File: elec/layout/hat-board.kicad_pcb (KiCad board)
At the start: 2 copper layers, 108 x 115.9 mm, 82 parts, among them P1 HatButtonAntenna, U1 _NXP_Semicon_PN5321A3HN_C106_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, U10 _OPSCO_Optoelectronics_SK6805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, U11 _OPSCO_Optoelectronics_SK6805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, U12 _OPSCO_Optoelectronics_SK6805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, U13 _OPSCO_Optoelectronics_SK6805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, U14 _OPSCO_Optoelectronics_SK6805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, U15 _OPSCO_Optoelectronics_SK6805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, U16 _OPSCO_Optoelectronics_SK6805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, U17 _OPSCO_Optoelectronics_SK6805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, U18 _OPSCO_Optoelectronics_SK6805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, U19 _OPSCO_Optoelectronics_SK6805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, U2 _OPSCO_Optoelectronics_SK6805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, U20 _OPSCO_Optoelectronics_SK6805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, U21 _OPSCO_Optoelectronics_SK6805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, U22 _OPSCO_Optoelectronics_SK6805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, U23 _OPSCO_Optoelectronics_SK6805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, U24 _OPSCO_Optoelectronics_SK6805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, U25 _Microchip_Tech_CAP1188_1_CP_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, U3 _OPSCO_Optoelectronics_SK6805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, U4 _OPSCO_Optoelectronics_SK6805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, U5 _OPSCO_Optoelectronics_SK6805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, U6 _OPSCO_Optoelectronics_SK6805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, U7 _OPSCO_Optoelectronics_SK6805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, U8 _OPSCO_Optoelectronics_SK6805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, U9 _OPSCO_Optoelectronics_SK6805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

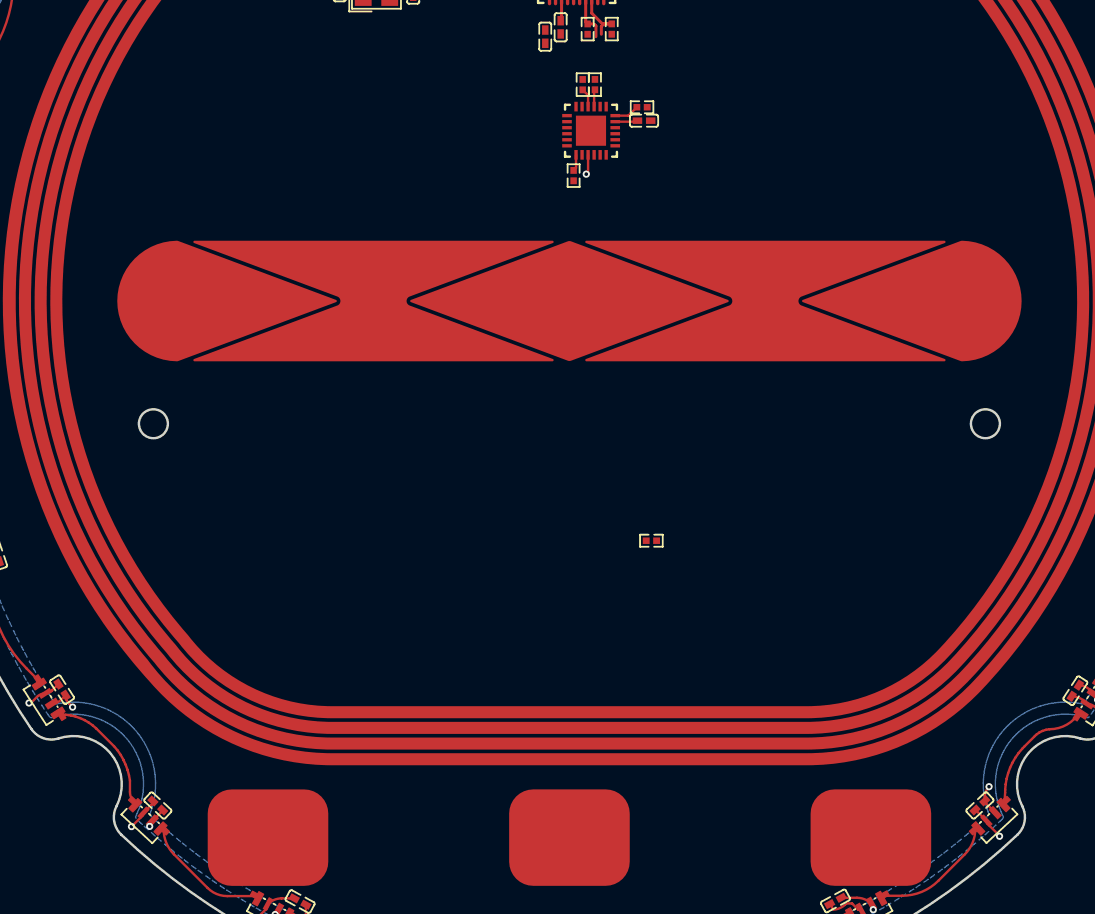
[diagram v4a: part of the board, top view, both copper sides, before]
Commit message: fixed hat-footprint
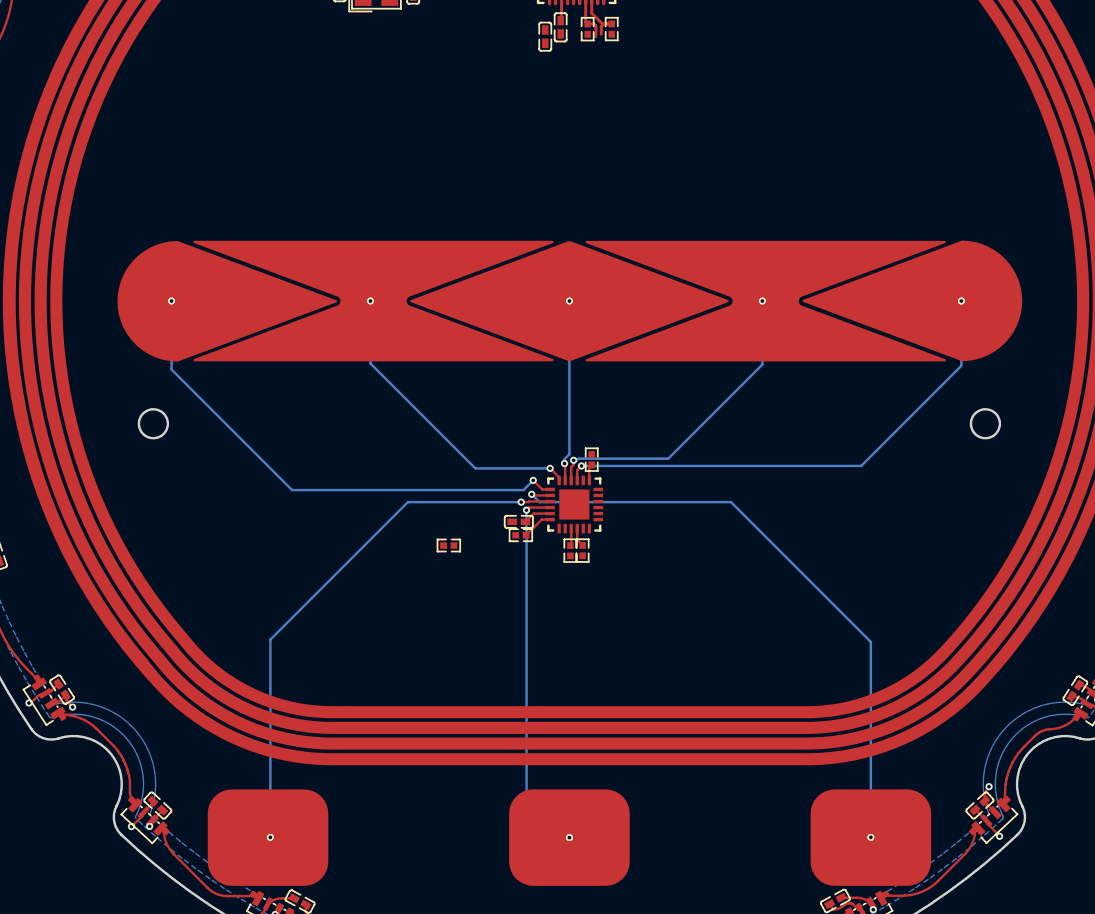
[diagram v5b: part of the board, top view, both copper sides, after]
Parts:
- moved R8 38.7 mm to (151.9, 111.8), turned to -90 degrees
- moved R7 38.6 mm to (152.9, 111.8), turned to -90 degrees
- moved R10 36.9 mm to (147.8, 110.5), turned to 180 degrees
- moved C42 34.9 mm to (147.6, 109.4), turned to 180 degrees
- moved U25 31.0 mm to (152.2, 108.0), turned to 90 degrees
- moved R9 23.6 mm to (153.7, 104.3), turned to 90 degrees
- moved R6 16.8 mm to (141.8, 111.4), turned to 180 degrees
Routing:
- net next_button: track 0.00 -> 51.0 mm, vias 0 -> 2
- net prev_button: track 0.00 -> 44.5 mm, vias 0 -> 2
- net slider_0: track 0.00 -> 41.9 mm, vias 0 -> 2
- net slider_4: track 1.66 -> 41.7 mm, vias 1 -> 2
- net play_button: track 0.00 -> 30.7 mm, vias 0 -> 2
- net slider_3: track 0.00 -> 26.0 mm, vias 0 -> 2
- net slider_1: track 0.00 -> 25.0 mm, vias 0 -> 2
- net slider_2: track 0.00 -> 15.1 mm, vias 0 -> 2

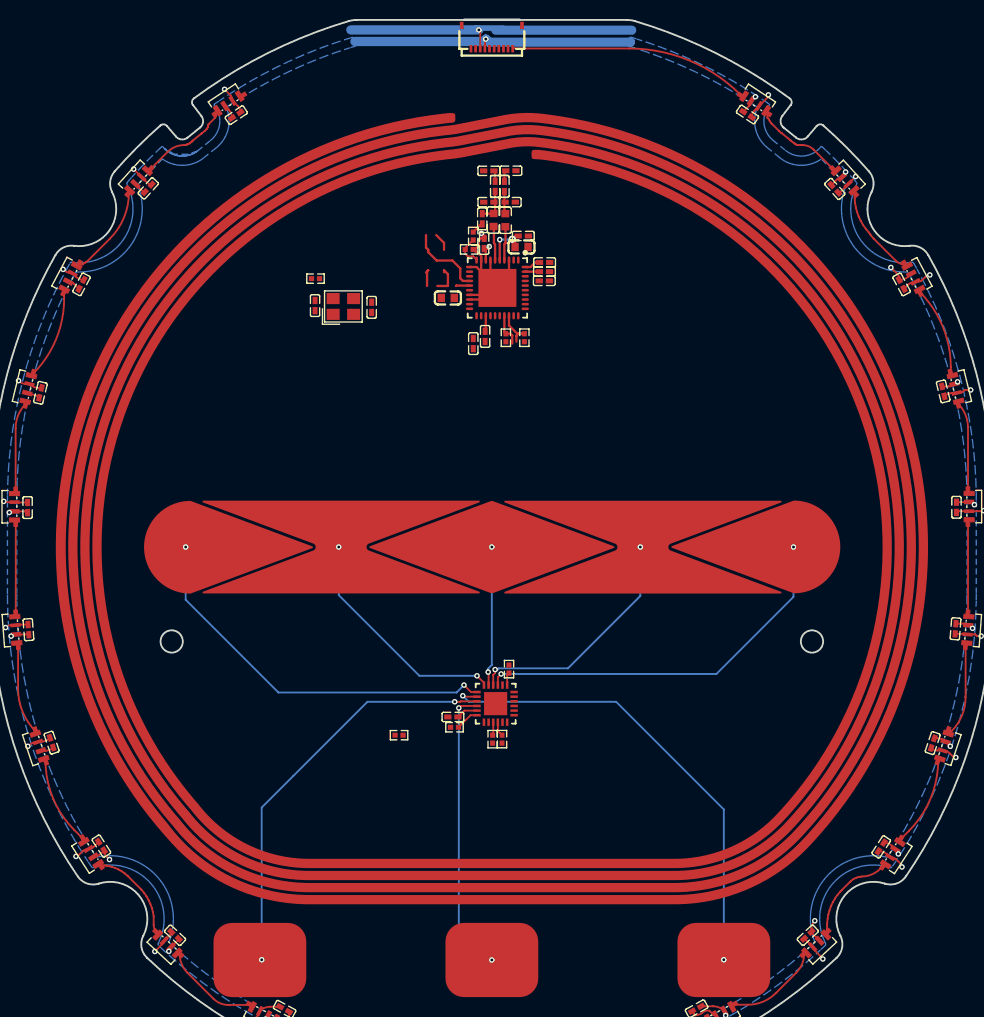
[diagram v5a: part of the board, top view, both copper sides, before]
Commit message: hat board layout complete
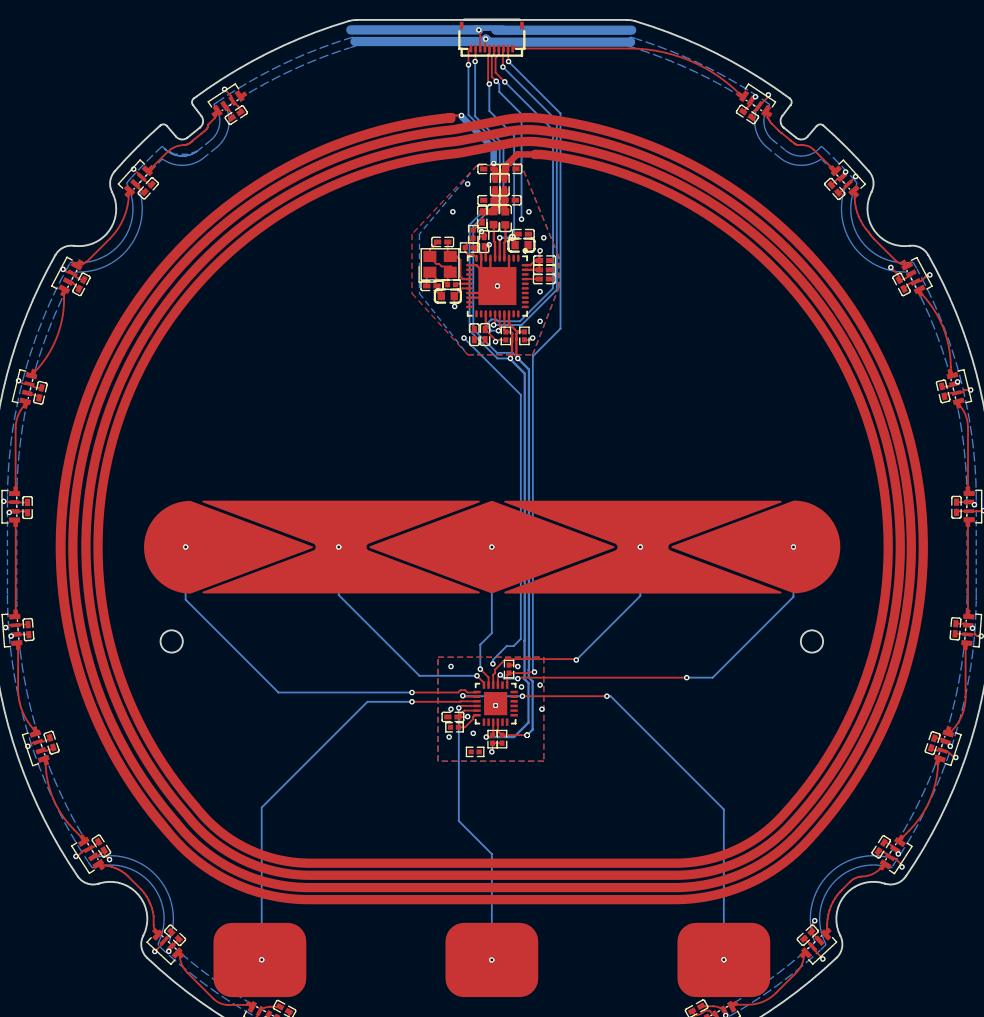
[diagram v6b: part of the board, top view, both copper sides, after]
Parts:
- moved R3 14.7 mm to (147.5, 62.9)
- moved C1 12.8 mm to (145.3, 63.0), turned to 0 degrees
- moved XTAL1 11.4 mm to (146.2, 60.7)
- moved C2 10.4 mm to (146.5, 58.2), turned to 180 degrees
- moved R6 8.40 mm to (150.0, 113.2)
- moved C11 0.97 mm to (149.9, 68.2), turned to 90 degrees
- moved C10 0.20 mm to (157.5, 60.3)
- moved C12 0.20 mm to (150.8, 55.6)
- moved C13 0.20 mm to (153.8, 50.4)
- moved C14 0.20 mm to (153.2, 52.1)
- moved C15 0.20 mm to (151.5, 50.4)
- moved C16 0.20 mm to (152.2, 52.1)
- moved C3 0.20 mm to (151.0, 58.2)
- moved C40 0.20 mm to (153.8, 53.8)
- moved C41 0.20 mm to (151.5, 53.8)
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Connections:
- C11 pad 2: nfc.power_vmid-lv -> lv
- C17 pad 2: lv -> gnd
- C18 pad 2: lv -> gnd
- C19 pad 2: lv -> gnd
- C2 pad 1: nfc-net-5 -> nfc-net-3
- C20 pad 2: lv -> gnd
- C21 pad 2: lv -> gnd
- C22 pad 2: lv -> gnd
- C23 pad 2: lv -> gnd
- C24 pad 2: lv -> gnd
- C25 pad 2: lv -> gnd
- C26 pad 2: lv -> gnd
- C27 pad 2: lv -> gnd
- C28 pad 2: lv -> gnd
- C29 pad 2: lv -> gnd
- C30 pad 2: lv -> gnd
- C31 pad 2: lv -> gnd
- C32 pad 2: lv -> gnd
- C33 pad 2: lv -> gnd
- C34 pad 2: lv -> gnd
- C35 pad 2: lv -> gnd
- C36 pad 2: lv -> gnd
- C37 pad 2: lv -> gnd
- C38 pad 2: lv -> gnd
- C39 pad 2: lv -> gnd
- C42 pad 1: capacitive_sensor-net-4 -> power_3v3
- C42 pad 2: capacitive_sensor-net-3 -> gnd
- C7 pad 2: nfc.power_svdd-lv -> gnd
- FPC1 pad 3: lv -> gnd
- L1 pad 2: nfc-net-1 -> nfc-net-2
- L2 pad 2: nfc-net-6 -> nfc-net-5
- R1 pad 2: hv -> power_3v3
- R10 pad 1: capacitive_sensor-net-2 -> capacitive_sensor-net
- R10 pad 2: capacitive_sensor.reset-lv -> gnd
- R2 pad 2: hv -> power_3v3
- R3 pad 2: nfc-net-3 -> nfc-net-6
- R4 pad 2: nfc-net-2 -> nfc-net-1
- R5 pad 2: nfc-net-2 -> nfc-net-1
- R6 pad 2: capacitive_sensor.address-lv -> gnd
- R7 pad 1: capacitive_sensor-net -> i2c_scl
- R7 pad 2: capacitive_sensor.i2c-hv -> power_3v3
- R8 pad 1: capacitive_sensor-net-1 -> i2c_sda
- R8 pad 2: capacitive_sensor.i2c-hv -> power_3v3
- R9 pad 2: hv-1 -> power_3v3
- U1 pad 10: nfc-net-2 -> nfc-net-1
- U1 pad 14: nfc-net-5 -> nfc-net-3
- U1 pad 15: nfc-net-3 -> nfc-net-6
- U1 pad 4: nfc-net-1 -> nfc-net-2
- U1 pad 6: nfc-net-6 -> nfc-net-5
- U10 pad 1: signal-10 -> signal-1
- U10 pad 2: lv -> gnd
- U10 pad 4: signal-2 -> signal-16
- U11 pad 1: signal-16 -> signal
- U11 pad 2: lv -> gnd
- U11 pad 4: signal-10 -> signal-1
- U12 pad 1: signal-15 -> signal-9
- U12 pad 2: lv -> gnd
- U12 pad 4: signal-16 -> signal
- U13 pad 1: signal-13 -> signal-6
- U13 pad 2: lv -> gnd
- U13 pad 4: signal-14 -> signal-7
- U14 pad 1: signal-21 -> signal-8
- U14 pad 2: lv -> gnd
- U14 pad 4: signal-15 -> signal-9
- U15 pad 1: signal-5 -> signal-21
- U15 pad 2: lv -> gnd
- U15 pad 4: signal-21 -> signal-8
- U16 pad 2: lv -> gnd
- U16 pad 4: signal-5 -> signal-21
- U17 pad 1: signal-17 -> signal-12
- U17 pad 2: lv -> gnd
- U17 pad 4: signal-13 -> signal-6
- U18 pad 1: signal-9 -> signal-18
- U18 pad 2: lv -> gnd
- U18 pad 4: signal-17 -> signal-12
- U19 pad 1: signal-8 -> signal-5
- U19 pad 2: lv -> gnd
- U19 pad 4: signal-9 -> signal-18
- U2 pad 1: signal-14 -> signal-7
- U2 pad 2: lv -> gnd
- U20 pad 1: signal-7 -> signal-4
- U20 pad 2: lv -> gnd
- U20 pad 4: signal-8 -> signal-5
- U21 pad 1: signal-6 -> signal-11
- U21 pad 2: lv -> gnd
- U21 pad 4: signal-7 -> signal-4
- U22 pad 1: signal-20 -> signal-10
- U22 pad 2: lv -> gnd
- U22 pad 4: signal-6 -> signal-11
- U23 pad 1: signal-1 -> signal-13
- U23 pad 2: lv -> gnd
- U23 pad 4: signal-20 -> signal-10
- U24 pad 1: signal -> signal-15
- U24 pad 2: lv -> gnd
- U24 pad 4: signal-1 -> signal-13
- U25 pad 23: capacitive_sensor-net-4 -> power_3v3
- U25 pad 24: capacitive_sensor-net-2 -> capacitive_sensor-net
- U25 pad 25: capacitive_sensor-net-3 -> gnd
- U25 pad 3: capacitive_sensor-net-1 -> i2c_sda
- U25 pad 4: capacitive_sensor-net -> i2c_scl
- U3 pad 1: signal-4 -> signal-20
- U3 pad 2: lv -> gnd
- U3 pad 4: signal -> signal-15
- U4 pad 1: signal-18 -> signal-14
- U4 pad 2: lv -> gnd
- U4 pad 4: signal-4 -> signal-20
- U5 pad 1: signal-19 -> signal-3
- U5 pad 2: lv -> gnd
- U5 pad 4: signal-18 -> signal-14
- U6 pad 1: signal-12 -> signal-2
- U6 pad 2: lv -> gnd
- U6 pad 4: signal-19 -> signal-3
- U7 pad 1: signal-11 -> signal-19
- U7 pad 2: lv -> gnd
- U7 pad 4: signal-12 -> signal-2
- U8 pad 1: signal-3 -> signal-17
- U8 pad 2: lv -> gnd
- U8 pad 4: signal-11 -> signal-19
- U9 pad 1: signal-2 -> signal-16
- U9 pad 2: lv -> gnd
- U9 pad 4: signal-3 -> signal-17
- XTAL1 pad 3: nfc-net-5 -> nfc-net-3
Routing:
- net gnd: track 29.9 -> 196.0 mm, vias 1 -> 43
- net lv: track 104.1 -> 0.00 mm, vias 24 -> 0
- net i2c_sda: track 3.66 -> 91.9 mm, vias 0 -> 3
- net i2c_scl: track 4.67 -> 91.7 mm, vias 0 -> 4
- net power_3v3: track 12.3 -> 86.4 mm, vias 3 -> 12
- net touch_irq: track 1.38 -> 75.0 mm, vias 0 -> 2
- net reset: track 0.00 -> 40.7 mm, vias 0 -> 2
- net nfc_irq: track 0.00 -> 37.8 mm, vias 0 -> 2
- net antenna_n: track 1.18 -> 9.86 mm, vias 0 -> 2
- net nfc-net-5: track 8.31 -> 3.91 mm
- net antenna_p: track 1.20 -> 5.51 mm
- net nfc-net-3: track 1.49 -> 5.80 mm
- net nfc.oscillator-net: track 3.22 -> 6.65 mm
- net capacitive_sensor-net-2: track 2.53 -> 0.00 mm
- net nfc-net-6: track 3.91 -> 1.49 mm
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- added copper zone on F.Cu, net gnd
- added copper zone on In2.Cu, net gnd
- added copper zone on B.Cu, net power_3v3
- added copper zone on In1.Cu, net power_3v3
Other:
- copper layers 2 -> 4
